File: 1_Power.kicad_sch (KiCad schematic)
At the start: 35 parts, among them Q201 IRLZ44N, Q202 IRLZ44N, U201 BQ24005, U202 LM74700, U203 LM74700, U205 LMR51430, U206 TPS7A2033PDBVR, U207 TLV75733PDBV

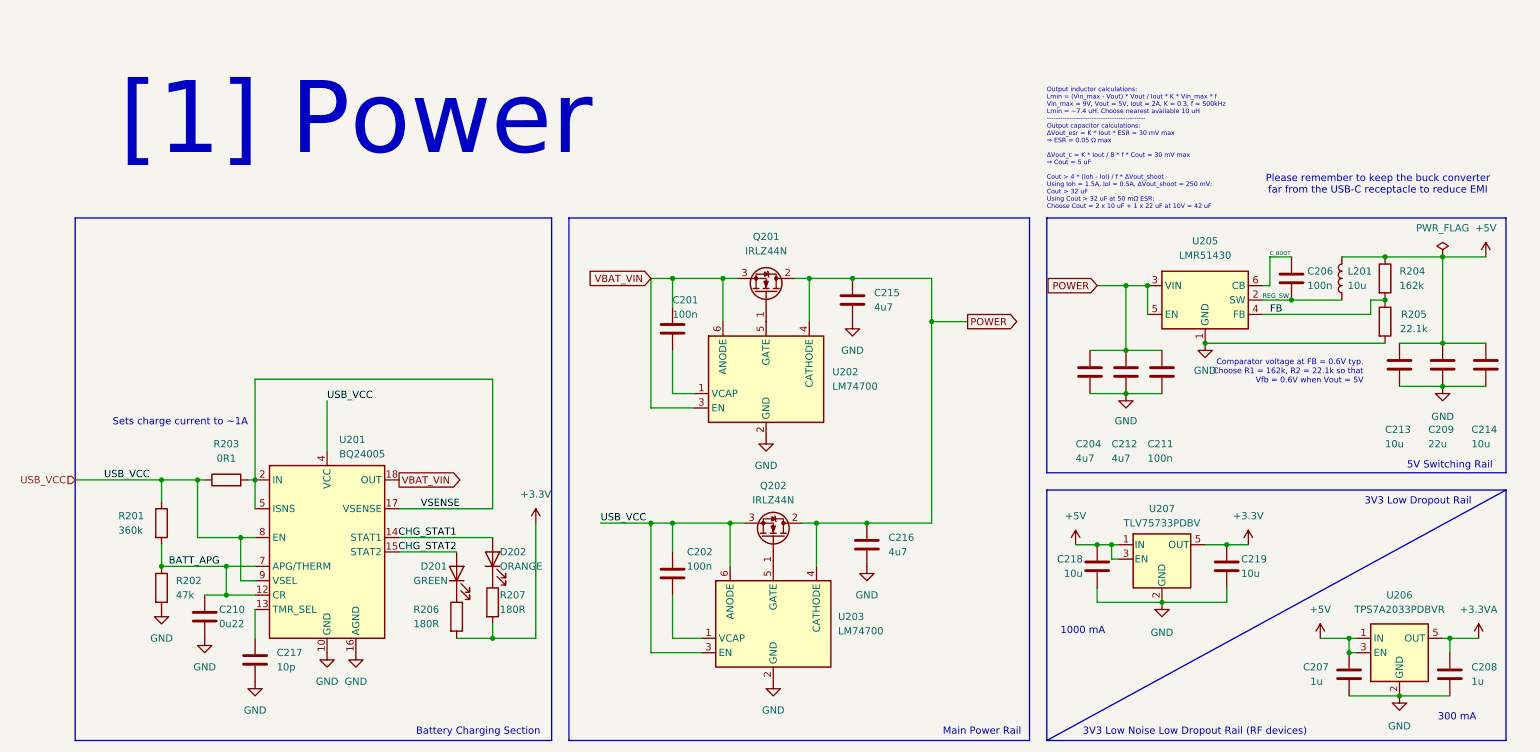
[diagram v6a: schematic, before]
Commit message: Continued connections for the new NAV
Added continuity sensing through a 8:1 mux
Restructured schematic so that everything actually fits in page 4
Updated CubeMX (ioc) file with pinout
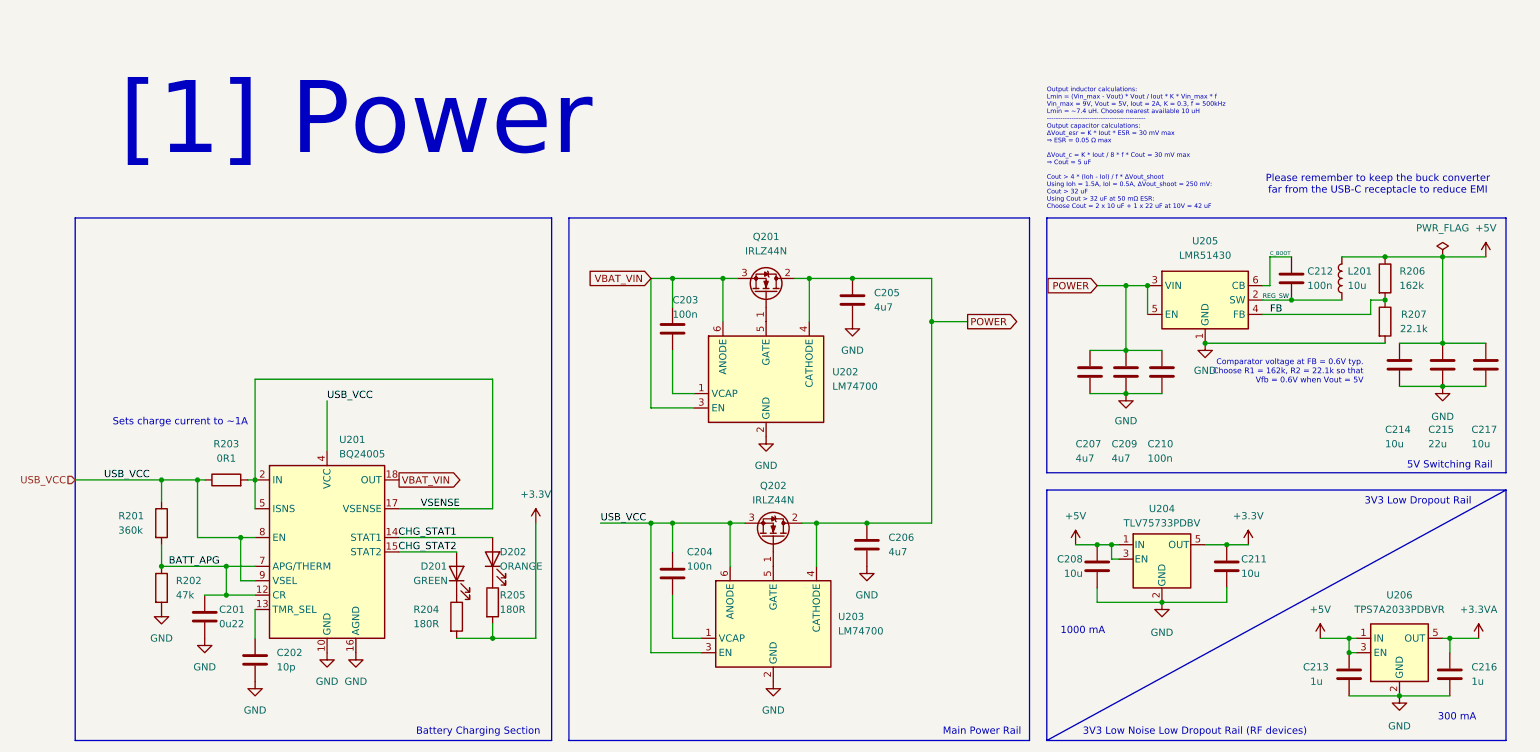
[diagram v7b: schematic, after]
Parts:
- renumbered C210 to C201, C217 to C202, C201 to C203, C202 to C204, C215 to C205, C216 to C206, C204 to C207, C218 to C208, C212 to C209, C211 to C210, C219 to C211, C206 to C212, C207 to C213, C213 to C214, C209 to C215, C208 to C216, C214 to C217, R206 to R204, R207 to R205, R204 to R206, R205 to R207, U207 to U204

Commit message: Finished restructuring schematic
Most components that were on page 3 are now in their own page
Added high-frequency 4.7 uF capacitor to servo power line
Continuity sensing on pyrochannels is multiplexed to one ADC on NAV.
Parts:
- L201: footprint Inductor_SMD:L_12x12mm_H8mm -> Inductor_SMD:L_Sunlord_SWPA8040S
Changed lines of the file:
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@@
 			)
 		)
-		(property "Footprint" "Inductor_SMD:L_12x12mm_H8mm"
+		(property "Footprint" "Inductor_SMD:L_Sunlord_SWPA8040S"
 			(at 245.11 67.31 0)
 			(hide yes)
